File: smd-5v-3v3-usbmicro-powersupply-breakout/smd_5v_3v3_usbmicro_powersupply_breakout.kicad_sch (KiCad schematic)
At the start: 13 parts, among them J1 USB_B_Micro, J2 THT 5V Jumper, J3 THT 3V3 Jumper, J4 SMD 5V Pad, J5 SMD 3V3 Pad, J6 SMD GND Pad, U1 LMS1585AIS-3.3

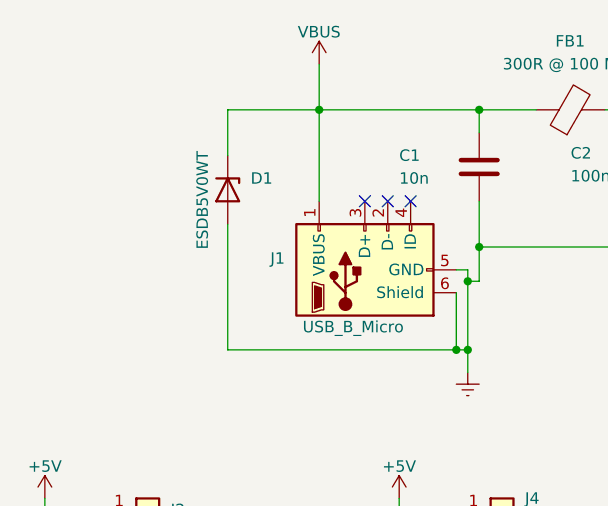
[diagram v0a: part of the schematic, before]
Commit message: Update tvs diode part number
- Mouser incorrectly listed a bidrectional diode as a unidirectional one
- Corrected the part number to a unidirectional TVS diode with similar
  specs
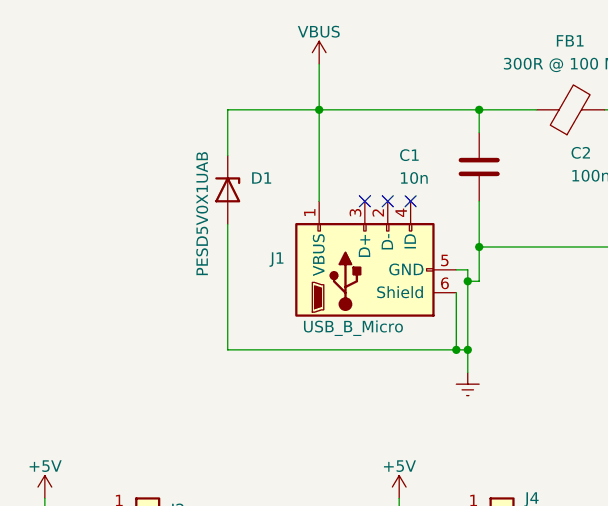
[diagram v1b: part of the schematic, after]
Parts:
- D1: value ESDB5V0WT -> PESD5V0X1UAB; MPN ESDB5V0WT -> PESD5V0X1UAB,115
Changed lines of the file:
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@@
 			)
 		)
-		(property "Value" "ESDB5V0WT"
+		(property "Value" "PESD5V0X1UAB"
 			(at 39.116 56.642 0)
 			(effects
@@
 			)
 		)
-		(property "MPN" "ESDB5V0WT"
+		(property "MPN" " PESD5V0X1UAB,115"
 			(at 41.91 60.96 0)
 			(effects

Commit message: Correct spacing in part numbers (smd 5v/3v3 psu)
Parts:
- D1: MPN PESD5V0X1UAB,115 -> PESD5V0X1UAB,115
- J1: MPN 10118194-0001LF -> 10118194-0001LF
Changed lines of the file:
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@@
 			)
 		)
-		(property "MPN" " PESD5V0X1UAB,115"
+		(property "MPN" "PESD5V0X1UAB,115"
 			(at 41.91 60.96 0)
 			(effects
@@
 			)
 		)
-		(property "MPN" " 10118194-0001LF"
+		(property "MPN" "10118194-0001LF"
 			(at 57.15 69.85 0)
 			(effects
